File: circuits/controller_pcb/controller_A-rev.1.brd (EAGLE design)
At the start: 38.8 x 16 mm, 54 parts, among them IC1 DS1820, J3 USB-MICROB", Q2 FDN340P, Q3 SI2333DS, Q5 BSS138, U1 ATMEGA328P_TQFP, U2 MIC5219 5V

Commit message: Updated controller Version A to Revision 1 - UNTESTED
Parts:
- removed U$3, U$4: 504050, con-molex-picolock:504050
- added U6, U7: 504050, con-molex-picolock:504050
- renumbered U$1 to U5, U$10 to U8, U$2 to U3, U$5 to U9, U$6 to X1, U$8 to U4, U$9 to X2
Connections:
- removed net N$7: TP1.TP, U$3.P$4, U$4.P$4
- new net AUX: TP1.TP, U6.P$4, U7.P$4
- net DATA: now also U6.P$3, U7.P$3; no longer U$3.P$3, U$4.P$3
- net GND: now also U6.P$1, U7.P$1; no longer U$3.P$1, U$4.P$1
- net VCC: now also U6.P$2, U7.P$2; no longer U$3.P$2, U$4.P$2
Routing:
- net N$7: track 15.1 -> 0.00 mm, vias 1 -> 0
- net AUX: track 0.00 -> 15.1 mm, vias 0 -> 1
- net VDD: track 12.5 -> 11.7 mm
- net GND: track 175.6 -> 175.0 mm
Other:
- board text added: "5V"
- board text added: "A - Rev. 1"
- board text added: "AUX"
- board text added: "DAT"
- board text added: "GND"
- board text added: "INT"
- board text added: "SCL"
- board text added: "SDA"
- board text added: "VCC"

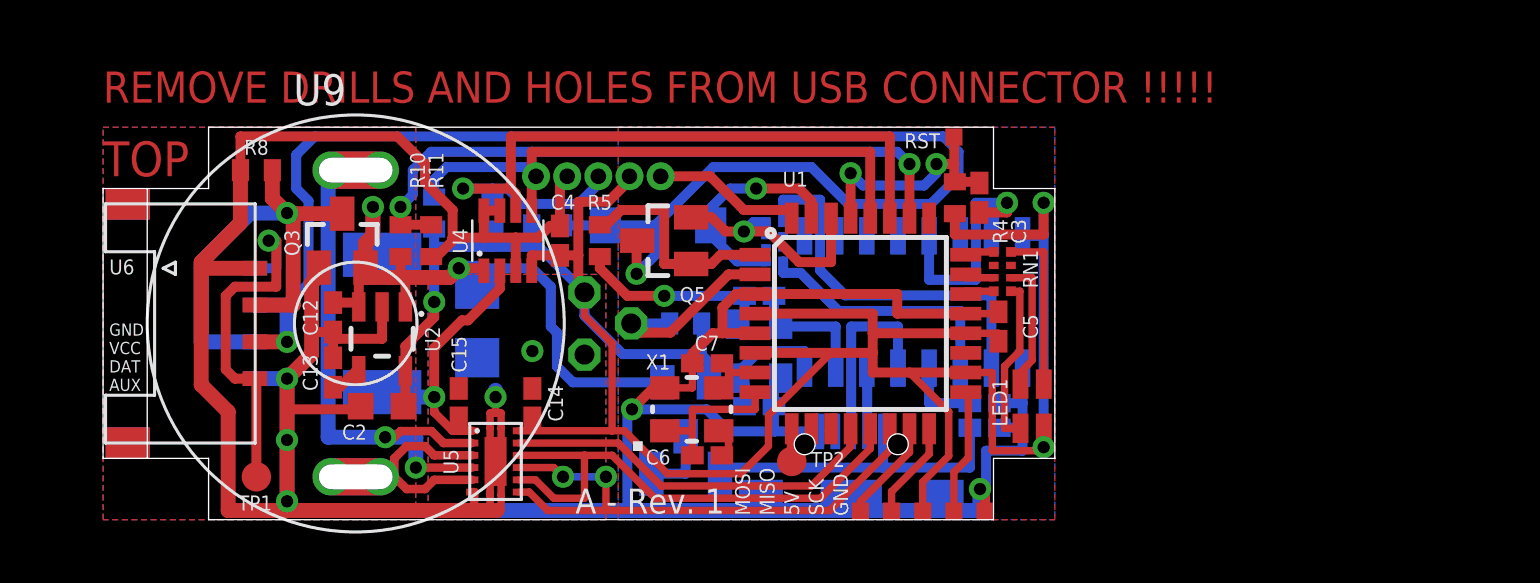
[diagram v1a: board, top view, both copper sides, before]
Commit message: Updated Q1 and replaced schottky diode - UNTESTED
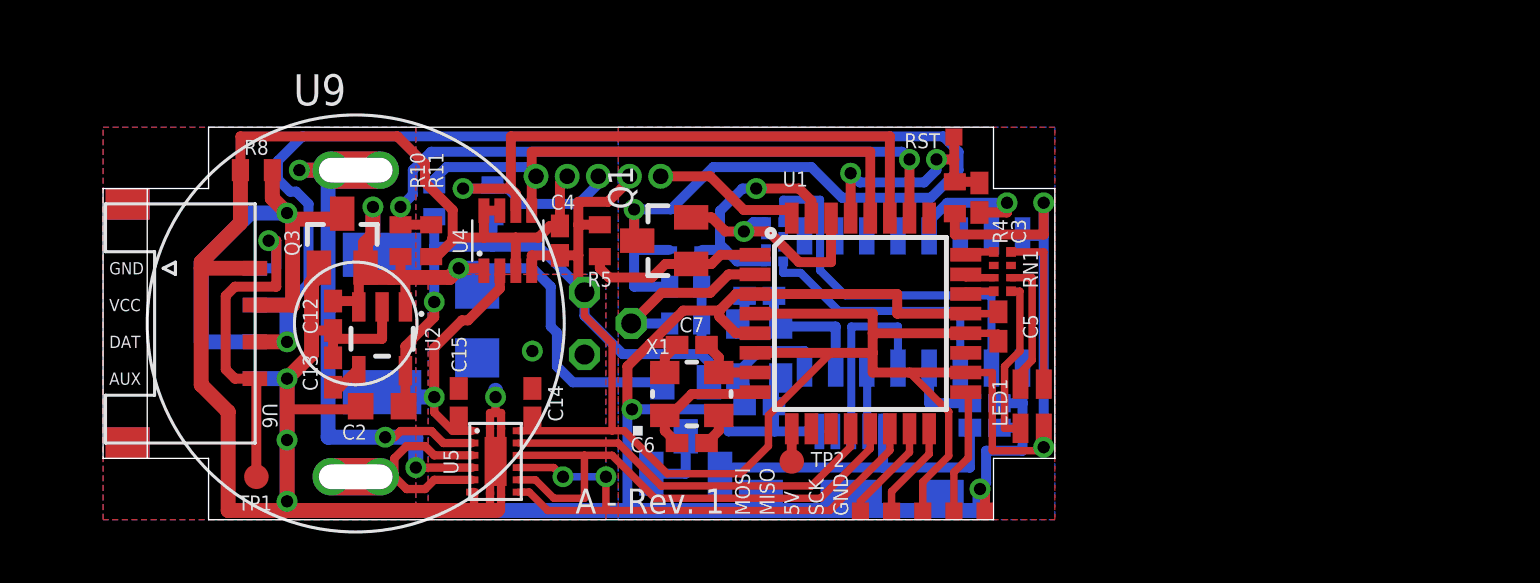
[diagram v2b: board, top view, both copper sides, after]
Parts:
- removed D1: IN5819, SparkFun-DiscreteSemi:SMA-DIODE
- removed J3: USB-MICROB", SparkFun-Connectors:USB-B-MICRO-SMD_V03
- removed Q5: BSS138, transistor-fet:SOT23
- added J1: (no value), ch340g:USB-B-MICRO-SMD_V03-NOHOLES
- added Q1: FDN340P, transistor-fet:SSOT-3
- added Z1: BAT41KFILM, schottky:SOD-523
- C11: value 100n -> 1u
- RN1, RN2: value (none) -> 1k
- TP1, TP2: value PTR1TP12R -> PTR1TP10R; device testpad:TP12R -> testpad:TP10R
- moved R6 6.16 mm to (23.8, 9.50), turned to 0 degrees
- moved C7 0.98 mm to (24.0, 7.12)
- moved C6 0.80 mm to (24.0, 3.12)
- moved X1 0.62 mm to (24.0, 5.12)
- moved R2 0.50 mm to (15.9, 13.0)
- moved R3 0.50 mm to (13.5, 13.0)
- moved C12 0.06 mm to (9.38, 8.31)
- turned R5 to 270 degrees
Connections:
- net 5V: now also R5.1
- net D+: now also J1.D+; no longer J3.D+
- net D-: now also J1.D-; no longer J3.D-
- net DATA: now also Q1.3, Z1.P$1; no longer D1.A, Q5.3
- net DIR: now also Q1.1; no longer Q5.1
- net GND: now also J1.GND, J1.SHIELD1, J1.SHIELD2, J1.SHIELD3; no longer J3.GND, J3.SHIELD1, J3.SHIELD2, J3.SHIELD3, R5.1
- net N$10: now also J1.VBUS; no longer J3.VBUS
- net RX: now also Q1.2; no longer Q5.2
- net TX: now also Z1.P$2; no longer D1.C
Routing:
- net N$5: track 9.86 -> 5.84 mm
- net GND: track 175.0 -> 171.0 mm, vias 8 -> 7
- net 5V: track 108.7 -> 111.2 mm
- net MOT+: track 24.0 -> 26.5 mm, vias 2 -> 3
- net DIR: track 8.94 -> 7.35 mm
- net DATA: track 61.6 -> 62.7 mm
- net N$1: track 6.26 -> 5.41 mm
- net SCL: track 24.3 -> 23.8 mm
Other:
- board text removed: "REMOVE DRILLS AND HOLES FROM USB CONNECTOR !!!!!"
- board text removed: "TOP"

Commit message: Updated controller PCB - Tested and working
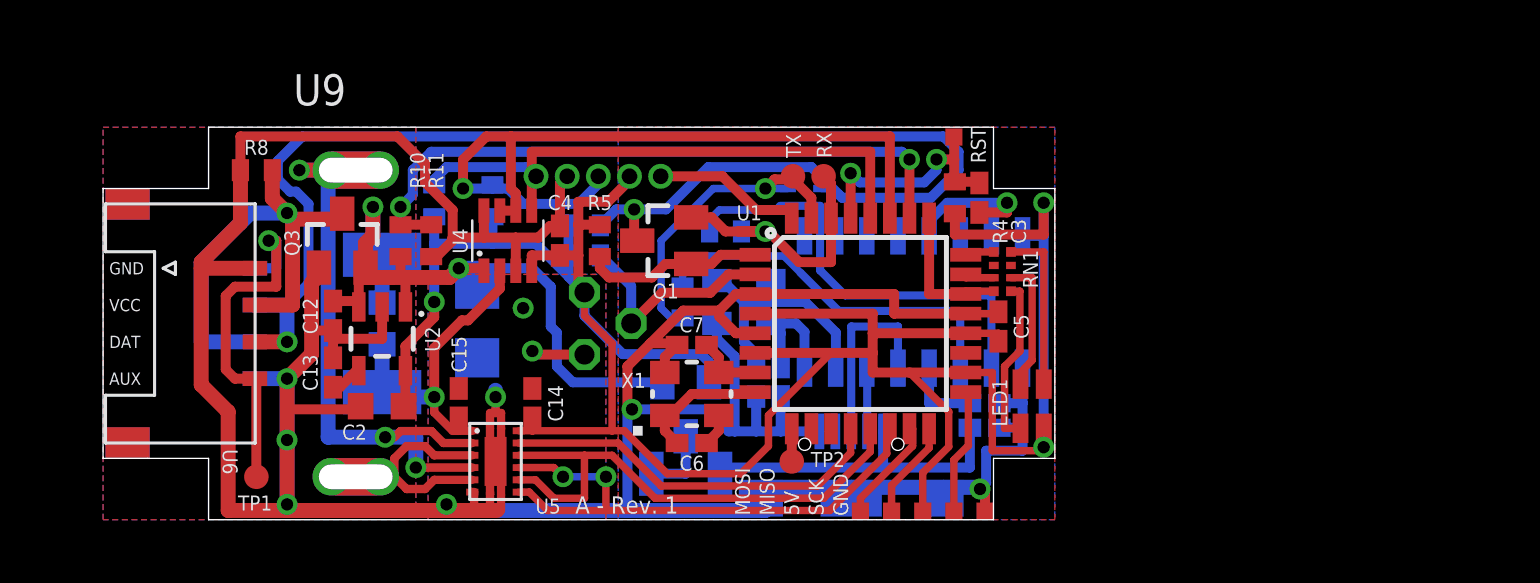
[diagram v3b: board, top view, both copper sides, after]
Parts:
- removed RN2: 1k, resistor-dil:YC124
- added R1: 0.1, rcl:R0603
- added R12, R13: 1k, rcl:R0402
- added RX, TX: PTR1TP10R, testpad:TP10R
- J1: device ch340g:USB-B-MICRO-SMD_V03-NOHOLES -> ch340g:USB-B-MICRO-SMD_V03
- Q1: value FDN340P -> NX3008PBK
- Q3: value SI2333DS -> DMP3099L-7
- R10: value (none) -> 18k
- R11: value (none) -> 13k
- moved Z1 5.45 mm to (28.6, 13.5), turned to 180 degrees
- moved R7 4.97 mm to (19.6, 10.8), turned to 180 degrees
- moved R6 4.82 mm to (19.6, 12.0), turned to 180 degrees
- moved C10 3.50 mm to (26.6, 5.62), turned to 270 degrees
- moved X2 2.10 mm to (26.1, 8.88), turned to 0 degrees
- moved C9 1.33 mm to (27.6, 5.62), turned to 270 degrees
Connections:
- net GND: no longer U4.7
- net LED_R: now also U1.25
- net N$15: now also R12.2; no longer RN2.8
- net N$6: now also R13.2; no longer RN2.5
- net RX: now also R13.1, RX.TP; no longer RN2.4
- net SDA: now also U4.7
- net TX: now also R12.1, TX.TP; no longer RN2.1
- net VDD: now also R1.1
- net VIN: now also R1.2
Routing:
- net GND: track 171.0 -> 176.2 mm, vias 7 -> 9
- net N$15: track 10.7 -> 15.6 mm
- net N$8: track 5.30 -> 10.0 mm
- net LED_R: track 1.26 -> 5.85 mm
- net TX: track 9.49 -> 13.2 mm
- net DATA: track 62.7 -> 59.1 mm
- net RX: track 9.56 -> 12.2 mm
- net N$6: track 15.7 -> 18.2 mm
- net SDA: track 30.4 -> 32.6 mm
- net VIN: track 29.3 -> 31.2 mm
- net VDD: track 11.7 -> 13.7 mm
- net 1WIRE: track 7.45 -> 9.18 mm
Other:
- board text added: "TOP"
